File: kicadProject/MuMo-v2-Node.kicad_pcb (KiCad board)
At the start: 2 copper layers, 52 x 50.3 mm, 77 parts, among them Q1 PJC7400, SW1 Reset, U1 MCP73123, U2 LoRa-E5, U3 CP2102N, U4 eInk_Display_1.54"200x200px, U5 BME680, U6 TSL25911, U7 BR24G512FVT-5AE2, U8 BR24G512FVT-5AE2

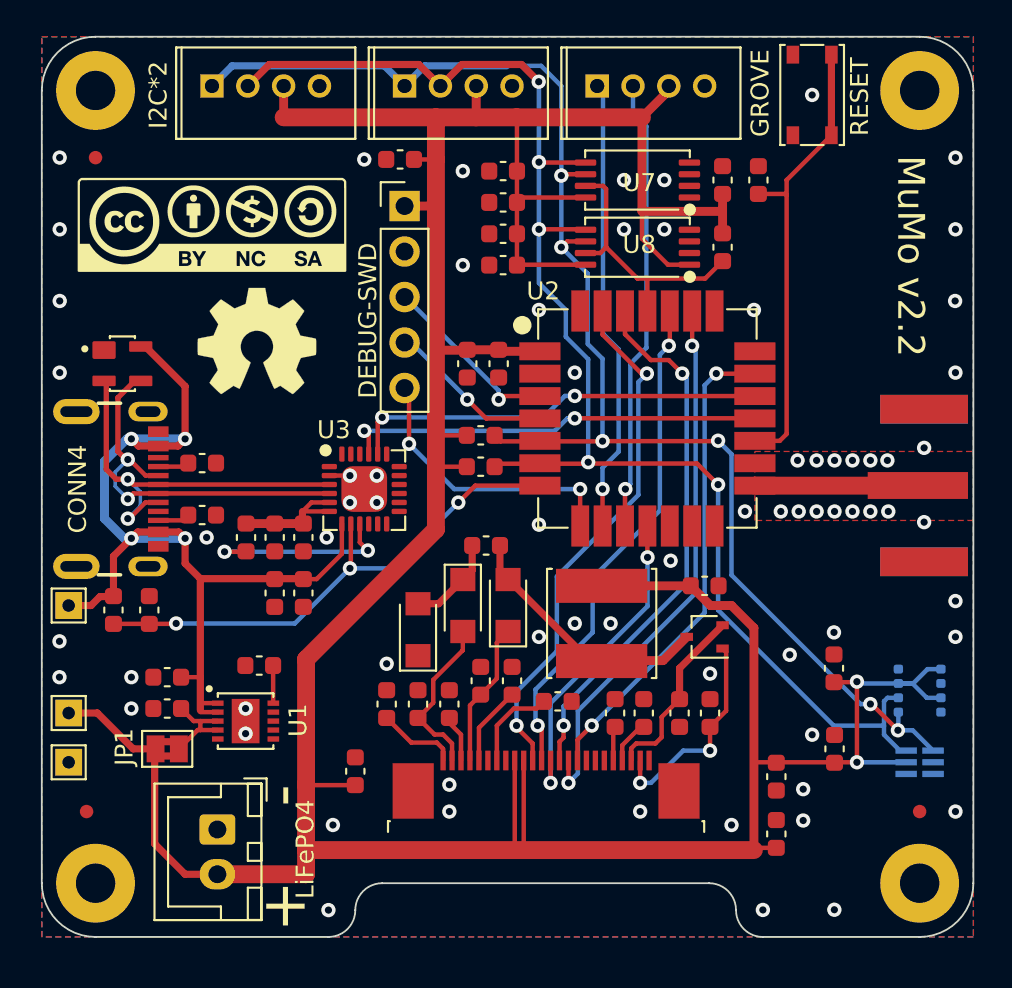
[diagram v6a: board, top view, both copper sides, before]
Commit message: V2.4
Updated to Kicad V7
* small design improvements, resolving the DRC of V7
* ready for production at Aisler
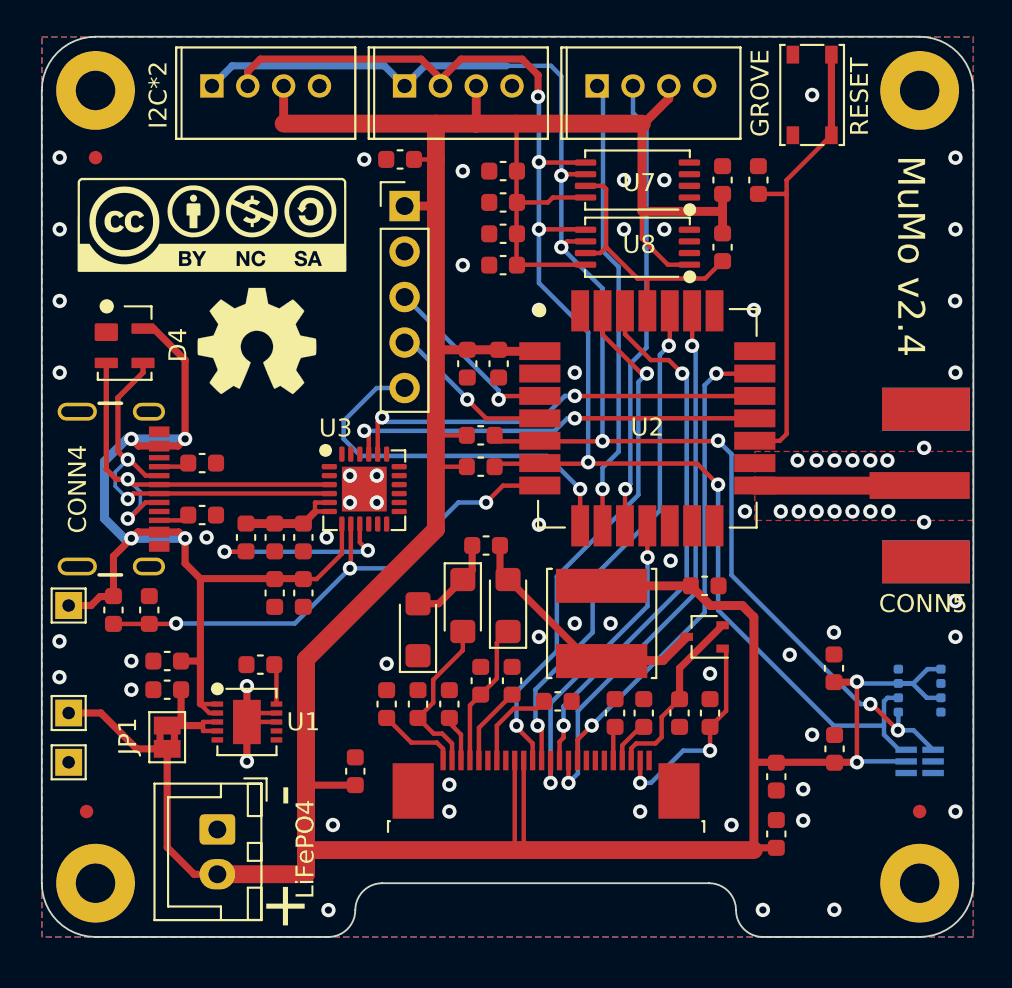
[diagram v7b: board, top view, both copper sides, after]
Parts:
- added G***: LOGO, thisProjectLibrary:logoMoMu20mm, B.Cu at (179.4, 72.0)
- added G***: LOGO, thisProjectLibrary:logoUA30mm, B.Cu at (179.4, 83.6)
- CONN4: value Molex-2171790001 -> 217179-0001
- CONN5: value External Antenna -> Conn_Coaxial_Power
- U1: value MCP73123 -> MCP73123T-22SI/MF; footprint thisProjectLibrary:DFN10 -> thisProjectLibrary:DFN10 - MCP73123
- U3: value CP2102N -> CP2102N-Axx-xQFN24
- moved G*** 2.77 mm to (170.4, 94.0)
- moved C42 1.05 mm to (150.0, 94.0)
- moved D4 1.01 mm to (147.7, 74.8)
- moved C32 0.90 mm to (150.0, 92.4)
- moved JP1 0.65 mm to (150.0, 96.7), turned to -90 degrees
- moved CONN5 0.10 mm to (194.8, 82.6)
- moved U1 0.09 mm to (154.5, 95.8), turned to -90 degrees
- moved R2 0.08 mm to (155.2, 92.6)
- moved CONN4 0.05 mm to (144.8, 82.8)
- moved U6 0.05 mm to (192.0, 98.0)
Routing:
- net GND: track 1.15 -> 7.71 mm
- net SWO: track 15.9 -> 21.6 mm, vias 2 -> 1
- net I2C2-SDA: track 82.1 -> 83.7 mm
- net +5V: track 55.7 -> 56.6 mm
- net D+: track 22.7 -> 23.6 mm
- net 3V: track 7.11 -> 6.22 mm
- net D-: track 21.6 -> 22.5 mm
- net Net-(JP1-A): track 5.45 -> 5.98 mm
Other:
- board text added: "MuMo v2.4"
- board text removed: "MuMo v2.2"
